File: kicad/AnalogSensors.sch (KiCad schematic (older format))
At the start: 8 parts, among them P201 Positive, P202 Negative

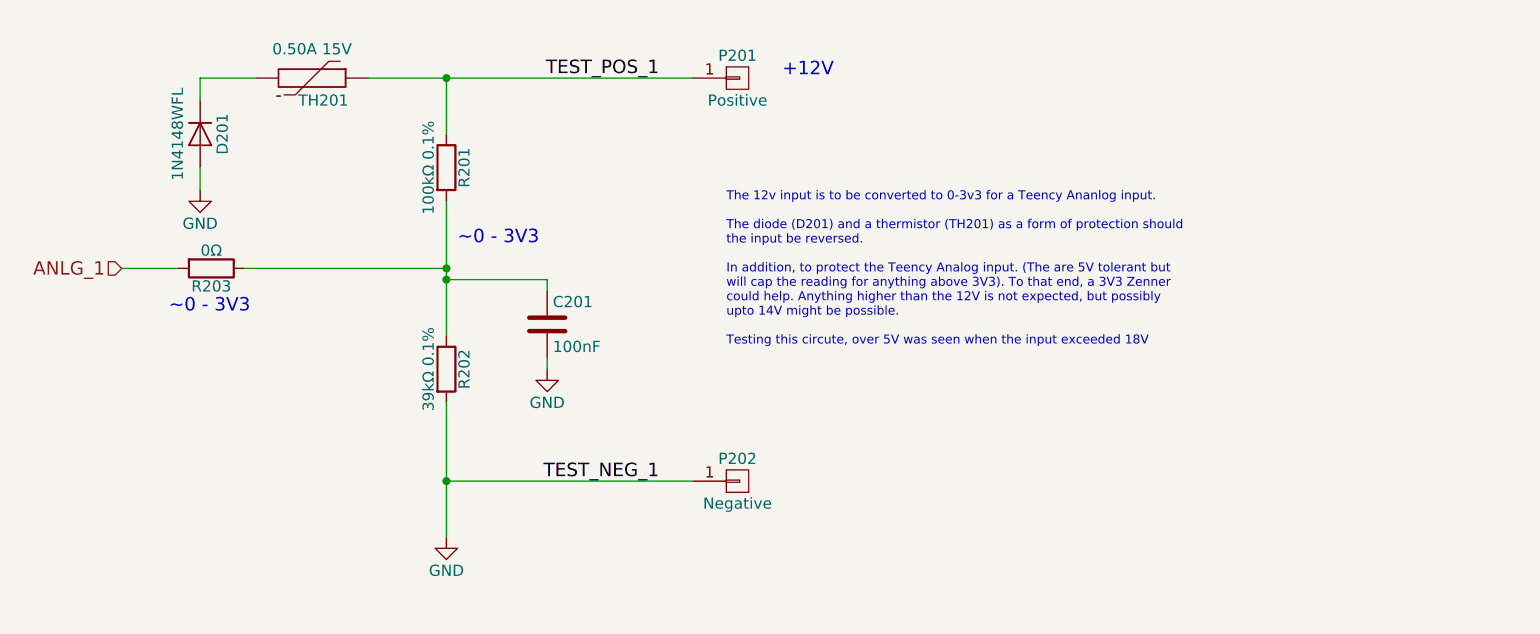
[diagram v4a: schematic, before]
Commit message: Small formatting changes on schematic for Forum questions
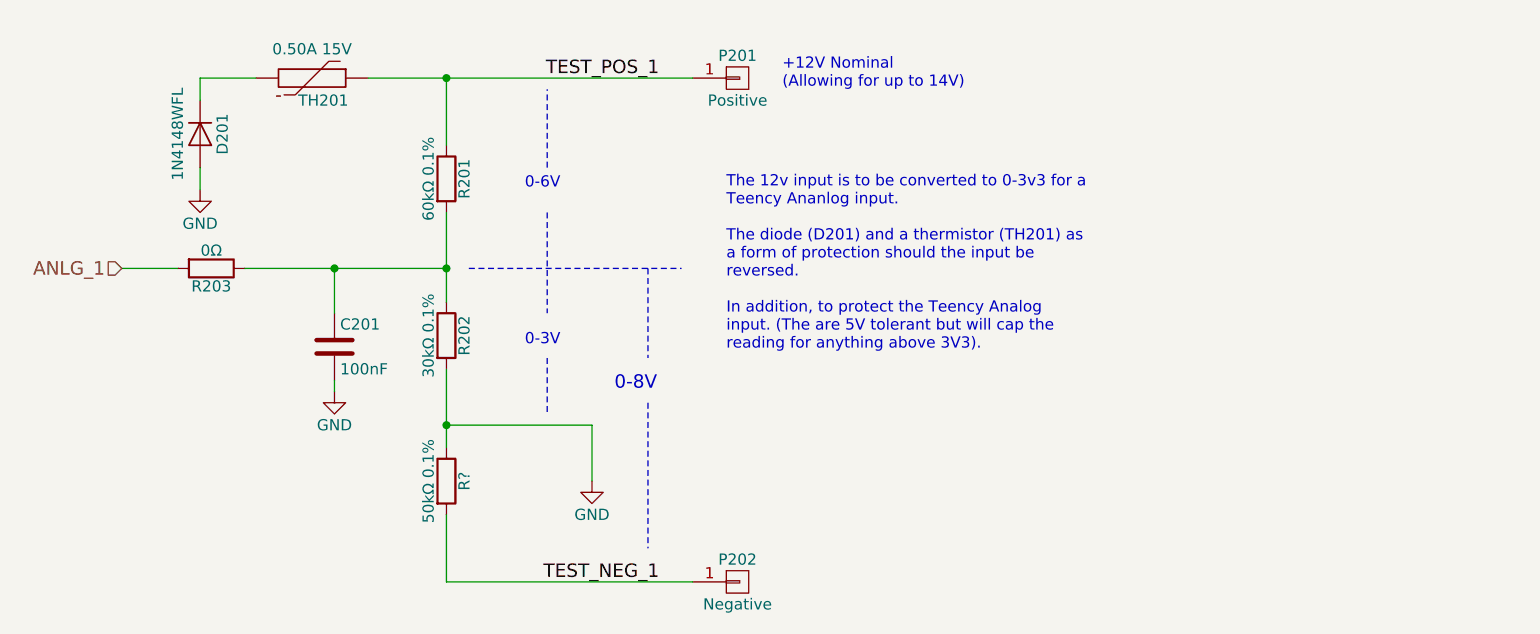
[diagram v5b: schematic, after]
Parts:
- added R?: 50kΩ 0.1%, Resistors_SMD:R_1206, symbol R
- R201: value 100kΩ 0.1% -> 60kΩ 0.1%
- R202: value 39kΩ 0.1% -> 30kΩ 0.1%
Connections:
- net GND: now also R?.1; no longer P202.1 (P1)
- new net TEST_NEG_1: P202.1 (P1), R?.2
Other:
- note added: "+12V Nominal\n(Allowing for up to 14V)"
- note added: "0-3V"
- note added: "0-6V"
- note added: "0-8V"
- note added: "\nThe 12v input is to be converted to 0-3v3 for a \nTeency Ananlog input.\n\nThe diode (D201) and a thermistor (TH201) as \na form of protection should the input be \nreversed.\n\nIn addition, to protect the Teency Analog \ninput. (The are 5V tolerant but will cap the \nreading for anything above 3V3).\n\n"
- note removed: "+12V"
- note removed: "\nThe 12v input is to be converted to 0-3v3 for a Teency Ananlog input.\n\nThe diode (D201) and a thermistor (TH201) as a form of protection should \nthe input be reversed.\n\nIn addition, to protect the Teency Analog input. (The are 5V tolerant but \nwill cap the reading for anything above 3V3). To that end, a 3V3 Zenner \ncould help. Anything higher than the 12V is not expected, but possibly \n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"
- note removed: "~~0 - 3V3"
- moved on the sheet: C201, P202, R201, R202
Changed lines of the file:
@@
 L R R201
 U 1 1 593EDD83
-P 3500 1800
-F 0 "R201" V 3580 1800 50  0000 C CNN
-F 1 "100kΩ 0.1%" V 3420 1800 50  0000 C CNN
-F 2 "Resistors_SMD:R_1206" V 3430 1800 50  0001 C CNN
-F 3 "" H 3500 1800 50  0000 C CNN
-F 4 "SPR-1206 100K" H 3500 1800 60  0001 C CNN "MPN"
-F 5 "Value" H 3500 1800 60  0001 C CNN "Link"
-	1    3500 1800
+P 3500 1850
+F 0 "R201" V 3580 1850 50  0000 C CNN
+F 1 "60kΩ 0.1%" V 3420 1850 50  0000 C CNN
+F 2 "Resistors_SMD:R_1206" V 3430 1850 50  0001 C CNN
+F 3 "" H 3500 1850 50  0000 C CNN
+F 4 "SPR-1206 100K" H 3500 1850 60  0001 C CNN "MPN"
+F 5 "Value" H 3500 1850 60  0001 C CNN "Link"
+	1    3500 1850
 	1    0    0    -1
 $EndComp
@@
 L R R202
 U 1 1 593EDD8A
-P 3500 2700
-F 0 "R202" V 3580 2700 50  0000 C CNN
-F 1 "39kΩ 0.1%" V 3420 2700 50  0000 C CNN
-F 2 "Resistors_SMD:R_1206" V 3430 2700 50  0001 C CNN
-F 3 "" H 3500 2700 50  0000 C CNN
-F 4 "SPR-1206 39,0K" H 3500 2700 60  0001 C CNN "MPN"
-F 5 "Value" H 3500 2700 60  0001 C CNN "Link"
-	1    3500 2700
+P 3500 2550
+F 0 "R202" V 3580 2550 50  0000 C CNN
+F 1 "30kΩ 0.1%" V 3420 2550 50  0000 C CNN
+F 2 "Resistors_SMD:R_1206" V 3430 2550 50  0001 C CNN
+F 3 "" H 3500 2550 50  0000 C CNN
+F 4 "SPR-1206 39,0K" H 3500 2550 60  0001 C CNN "MPN"
+F 5 "Value" H 3500 2550 60  0001 C CNN "Link"
+	1    3500 2550
 	1    0    0    -1
 $EndComp
@@
 L GND #PWR07
 U 1 1 593EDD91
-P 3500 3450
-F 0 "#PWR07" H 3500 3200 50  0001 C CNN
-F 1 "GND" H 3500 3300 50  0000 C CNN
-F 2 "" H 3500 3450 50  0000 C CNN
-F 3 "" H 3500 3450 50  0000 C CNN
-	1    3500 3450
-	1    0    0    -1
-$EndComp
-Text Label 4450 3200 2    60   ~ 0
+P 4150 3200
+F 0 "#PWR07" H 4150 2950 50  0001 C CNN
+F 1 "GND" H 4150 3050 50  0000 C CNN
+F 2 "" H 4150 3200 50  0000 C CNN
+F 3 "" H 4150 3200 50  0000 C CNN
+	1    4150 3200
+	1    0    0    -1
+$EndComp
+Text Label 4450 3650 2    60   ~ 0
 TEST_NEG_1
 Text Label 4450 1400 2    60   ~ 0
@@
 	0    1    1    0
 $EndComp
-Text Notes 5000 1400 0    60   ~ 0
-+12V
-Text Notes 2260 2455 0    60   ~ 0
-~~0 - 3V3
+Text Notes 5000 1450 0    50   ~ 0
++12V Nominal\n(Allowing for up to 14V)
 $Comp
 L C C201
 U 1 1 593EDDC1
-P 3950 2500
-F 0 "C201" H 3975 2600 50  0000 L CNN
-F 1 "100nF" H 3975 2400 50  0000 L CNN
-F 2 "Capacitors_SMD:C_0805" H 3988 2350 30  0001 C CNN
-F 3 "" H 3950 2500 60  0000 C CNN
-	1    3950 2500
+P 3000 2600
+F 0 "C201" H 3025 2700 50  0000 L CNN
+F 1 "100nF" H 3025 2500 50  0000 L CNN
+F 2 "Capacitors_SMD:C_0805" H 3038 2450 30  0001 C CNN
+F 3 "" H 3000 2600 60  0000 C CNN
+	1    3000 2600
 	1    0    0    -1
 $EndComp
@@
 L GND #PWR09
 U 1 1 593EDDCB
-P 3950 2700
-F 0 "#PWR09" H 3950 2450 50  0001 C CNN
-F 1 "GND" H 3950 2550 50  0000 C CNN
-F 2 "" H 3950 2700 50  0000 C CNN
-F 3 "" H 3950 2700 50  0000 C CNN
-	1    3950 2700
+P 3000 2800
+F 0 "#PWR09" H 3000 2550 50  0001 C CNN
+F 1 "GND" H 3000 2650 50  0000 C CNN
+F 2 "" H 3000 2800 50  0000 C CNN
+F 3 "" H 3000 2800 50  0000 C CNN
+	1    3000 2800
 	1    0    0    -1
 $EndComp
@@
 	3150 1400 4600 1400
 Wire Wire Line
-	3500 1400 3500 1650
+	3500 1400 3500 1700
 Connection ~ 3500 1400
 Wire Wire Line
-	3500 1950 3500 2550
-Wire Wire Line
-	3500 2850 3500 3450
-Wire Wire Line
-	3950 2650 3950 2700
-Wire Wire Line
-	3950 2300 3950 2350
-Wire Wire Line
-	3500 3200 4600 3200
-Connection ~ 3500 3200
+	3500 2000 3500 2400
+Wire Wire Line
+	3000 2750 3000 2800
+Wire Wire Line
+	3500 3650 4600 3650
 $Comp
 L CONN_01X01 P201
@@
 L CONN_01X01 P202
 U 1 1 594067C4
-P 4800 3200
-F 0 "P202" H 4800 3300 50  0000 C CNN
-F 1 "Negative" H 4800 3100 50  0000 C CNN
-F 2 "Pin_Headers:Pin_Header_Straight_1x01_Pitch2.54mm" H 4800 3200 60  0001 C CNN
-F 3 "" H 4800 3200 60  0000 C CNN
-	1    4800 3200
+P 4800 3650
+F 0 "P202" H 4800 3750 50  0000 C CNN
+F 1 "Negative" H 4800 3550 50  0000 C CNN
+F 2 "Pin_Headers:Pin_Header_Straight_1x01_Pitch2.54mm" H 4800 3650 60  0001 C CNN
+F 3 "" H 4800 3650 60  0000 C CNN
+	1    4800 3650
 	1    0    0    -1
 $EndComp
@@
 	2600 2250 3500 2250
 Connection ~ 3500 2250
-Wire Wire Line
-	3500 2300 3950 2300
-Connection ~ 3500 2300
-Text Notes 4750 2600 0    40   ~ 0
-\nThe 12v input is to be converted to 0-3v3 for a Teency Ananlog input.\n\nThe diode (D201) and a thermistor (TH201) as a form of protection should \nthe input be reversed.\n\nIn addition, to protect the Teency Analog input. (The are 5V tolerant but \nwill cap the reading for anything above 3V3). To that end, a 3V3 Zenner \ncould help. Anything higher than the 12V is not expected, but possibly \nupto 14V might be possible.\n\nTesting this circute, over 5V was seen when the input exceeded 18V
-Text Notes 3550 2150 0    60   ~ 0
-~~0 - 3V3
+Text Notes 4750 2700 0    50   ~ 0
+\nThe 12v input is to be converted to 0-3v3 for a \nTeency Ananlog input.\n\nThe diode (D201) and a thermistor (TH201) as \na form of protection should the input be \nreversed.\n\nIn addition, to protect the Teency Analog \ninput. (The are 5V tolerant but will cap the \nreading for anything above 3V3).\n\n
+Text Notes 3850 2600 0    50   ~ 0
+0-3V
+$Comp
+L R R?
+U 1 1 599477ED
+P 3500 3200
+F 0 "R?" V 3580 3200 50  0000 C CNN
+F 1 "50kΩ 0.1%" V 3420 3200 50  0000 C CNN
+F 2 "Resistors_SMD:R_1206" V 3430 3200 50  0001 C CNN
+F 3 "" H 3500 3200 50  0000 C CNN
+F 4 "SPR-1206 39,0K" H 3500 3200 60  0001 C CNN "MPN"
+F 5 "Value" H 3500 3200 60  0001 C CNN "Link"
+	1    3500 3200
+	1    0    0    -1
+$EndComp
+Wire Wire Line
+	3500 2700 3500 3050
+Wire Wire Line
+	3500 3350 3500 3650
+Wire Wire Line
+	3500 2950 4150 2950
+Wire Wire Line
+	4150 2950 4150 3200
+Connection ~ 3500 2950
+Wire Wire Line
+	3000 2450 3000 2250
+Connection ~ 3000 2250
+Wire Notes Line
+	4400 2250 4400 2650
+Wire Notes Line
+	4400 2850 4400 3500
+Text Notes 4250 2800 0    60   ~ 0
+0-8V
+Wire Notes Line
+	3600 2250 4550 2250
+Wire Notes Line
+	3950 2000 3950 2450
+Wire Notes Line
+	3950 2650 3950 2900
+Wire Notes Line
+	3950 1800 3950 1450
+Text Notes 3850 1900 0    50   ~ 0
+0-6V
 $EndSCHEMATC

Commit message: Enhanced display port connector and layout - Submit to OSH Park
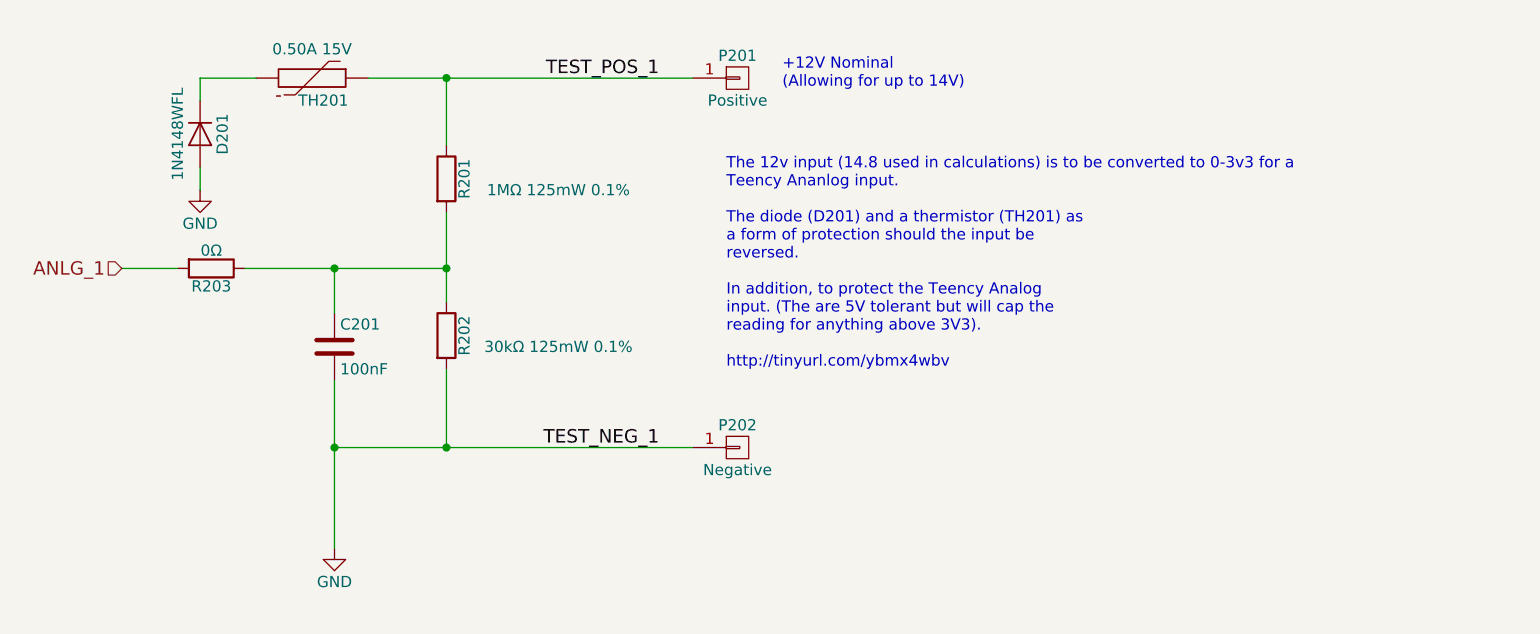
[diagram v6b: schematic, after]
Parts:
- removed R?: 50kΩ 0.1%, Resistors_SMD:R_1206, symbol R
- C201: footprint Capacitors_SMD:C_0805 -> Capacitors_SMD:C_0805_HandSoldering
- R201: value 60kΩ 0.1% -> 1MΩ 125mW 0.1%; footprint Resistors_SMD:R_1206 -> Resistors_SMD:R_1206_HandSoldering
- R202: value 30kΩ 0.1% -> 30kΩ 125mW 0.1%; footprint Resistors_SMD:R_1206 -> Resistors_SMD:R_1206_HandSoldering
- R203: footprint Resistors_SMD:R_0805 -> Resistors_SMD:R_0805_HandSoldering
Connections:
- net TEST_NEG_1 is gone; now on net GND: P202.1 (P1)
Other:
- note added: "\nThe 12v input (14.8 used in calculations) is to be converted to 0-3v3 for a \nTeency Ananlog input.\n\nThe diode (D201) and a thermistor (TH201) as \na form of protection should the input be \nreversed.\n\nIn addition, to protect the Teency Analog \ninput. (The are 5V tolerant but will cap the \nreading for anything above 3V3).\n\nhttp://tinyurl.com/ybmx4wbv"
- note removed: "0-3V"
- note removed: "0-6V"
- note removed: "0-8V"
- note removed: "\nThe 12v input is to be converted to 0-3v3 for a \nTeency Ananlog input.\n\nThe diode (D201) and a thermistor (TH201) as \na form of protection should the input be \nreversed.\n\nIn addition, to protect the Teency Analog \ninput. (The are 5V tolerant but will cap the \nreading for anything above 3V3).\n\n"
- moved on the sheet: P202
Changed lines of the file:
@@
 P 3500 1850
 F 0 "R201" V 3580 1850 50  0000 C CNN
-F 1 "60kΩ 0.1%" V 3420 1850 50  0000 C CNN
-F 2 "Resistors_SMD:R_1206" V 3430 1850 50  0001 C CNN
+F 1 "1MΩ 125mW  0.1%" H 4000 1800 50  0000 C CNN
+F 2 "Resistors_SMD:R_1206_HandSoldering" V 3430 1850 50  0001 C CNN
 F 3 "" H 3500 1850 50  0000 C CNN
 F 4 "SPR-1206 100K" H 3500 1850 60  0001 C CNN "MPN"
@@
 P 3500 2550
 F 0 "R202" V 3580 2550 50  0000 C CNN
-F 1 "30kΩ 0.1%" V 3420 2550 50  0000 C CNN
-F 2 "Resistors_SMD:R_1206" V 3430 2550 50  0001 C CNN
+F 1 "30kΩ 125mW  0.1%" H 4000 2500 50  0000 C CNN
+F 2 "Resistors_SMD:R_1206_HandSoldering" V 3430 2550 50  0001 C CNN
 F 3 "" H 3500 2550 50  0000 C CNN
 F 4 "SPR-1206 39,0K" H 3500 2550 60  0001 C CNN "MPN"
@@
 	1    0    0    -1
 $EndComp
-$Comp
-L GND #PWR07
-U 1 1 593EDD91
-P 4150 3200
-F 0 "#PWR07" H 4150 2950 50  0001 C CNN
-F 1 "GND" H 4150 3050 50  0000 C CNN
-F 2 "" H 4150 3200 50  0000 C CNN
-F 3 "" H 4150 3200 50  0000 C CNN
-	1    4150 3200
-	1    0    0    -1
-$EndComp
-Text Label 4450 3650 2    60   ~ 0
+Text Label 4450 3050 2    60   ~ 0
 TEST_NEG_1
 Text Label 4450 1400 2    60   ~ 0
@@
 F 0 "C201" H 3025 2700 50  0000 L CNN
 F 1 "100nF" H 3025 2500 50  0000 L CNN
-F 2 "Capacitors_SMD:C_0805" H 3038 2450 30  0001 C CNN
+F 2 "Capacitors_SMD:C_0805_HandSoldering" H 3038 2450 30  0001 C CNN
 F 3 "" H 3000 2600 60  0000 C CNN
 	1    3000 2600
@@
 L GND #PWR09
 U 1 1 593EDDCB
-P 3000 2800
-F 0 "#PWR09" H 3000 2550 50  0001 C CNN
-F 1 "GND" H 3000 2650 50  0000 C CNN
-F 2 "" H 3000 2800 50  0000 C CNN
-F 3 "" H 3000 2800 50  0000 C CNN
-	1    3000 2800
+P 3000 3500
+F 0 "#PWR09" H 3000 3250 50  0001 C CNN
+F 1 "GND" H 3000 3350 50  0000 C CNN
+F 2 "" H 3000 3500 50  0000 C CNN
+F 3 "" H 3000 3500 50  0000 C CNN
+	1    3000 3500
 	1    0    0    -1
 $EndComp
@@
 	3500 2000 3500 2400
 Wire Wire Line
-	3000 2750 3000 2800
-Wire Wire Line
-	3500 3650 4600 3650
+	3000 2750 3000 3500
 $Comp
 L CONN_01X01 P201
@@
 L CONN_01X01 P202
 U 1 1 594067C4
-P 4800 3650
-F 0 "P202" H 4800 3750 50  0000 C CNN
-F 1 "Negative" H 4800 3550 50  0000 C CNN
-F 2 "Pin_Headers:Pin_Header_Straight_1x01_Pitch2.54mm" H 4800 3650 60  0001 C CNN
-F 3 "" H 4800 3650 60  0000 C CNN
-	1    4800 3650
+P 4800 3050
+F 0 "P202" H 4800 3150 50  0000 C CNN
+F 1 "Negative" H 4800 2950 50  0000 C CNN
+F 2 "Pin_Headers:Pin_Header_Straight_1x01_Pitch2.54mm" H 4800 3050 60  0001 C CNN
+F 3 "" H 4800 3050 60  0000 C CNN
+	1    4800 3050
 	1    0    0    -1
 $EndComp
@@
 F 0 "R203" V 2530 2250 50  0000 C CNN
 F 1 "0Ω" V 2370 2250 50  0000 C CNN
-F 2 "Resistors_SMD:R_0805" V 2380 2250 50  0001 C CNN
+F 2 "Resistors_SMD:R_0805_HandSoldering" V 2380 2250 50  0001 C CNN
 F 3 "" H 2450 2250 50  0000 C CNN
 F 4 "Value" H 2450 2250 60  0001 C CNN "Link"
@@
 Connection ~ 3500 2250
 Text Notes 4750 2700 0    50   ~ 0
-\nThe 12v input is to be converted to 0-3v3 for a \nTeency Ananlog input.\n\nThe diode (D201) and a thermistor (TH201) as \na form of protection should the input be \nreversed.\n\nIn addition, to protect the Teency Analog \ninput. (The are 5V tolerant but will cap the \nreading for anything above 3V3).\n\n
-Text Notes 3850 2600 0    50   ~ 0
-0-3V
-$Comp
-L R R?
-U 1 1 599477ED
-P 3500 3200
-F 0 "R?" V 3580 3200 50  0000 C CNN
-F 1 "50kΩ 0.1%" V 3420 3200 50  0000 C CNN
-F 2 "Resistors_SMD:R_1206" V 3430 3200 50  0001 C CNN
-F 3 "" H 3500 3200 50  0000 C CNN
-F 4 "SPR-1206 39,0K" H 3500 3200 60  0001 C CNN "MPN"
-F 5 "Value" H 3500 3200 60  0001 C CNN "Link"
-	1    3500 3200
-	1    0    0    -1
-$EndComp
-Wire Wire Line
-	3500 2700 3500 3050
-Wire Wire Line
-	3500 3350 3500 3650
-Wire Wire Line
-	3500 2950 4150 2950
-Wire Wire Line
-	4150 2950 4150 3200
-Connection ~ 3500 2950
+\nThe 12v input (14.8 used in calculations) is to be converted to 0-3v3 for a \nTeency Ananlog input.\n\nThe diode (D201) and a thermistor (TH201) as \na form of protection should the input be \nreversed.\n\nIn addition, to protect the Teency Analog \ninput. (The are 5V tolerant but will cap the \nreading for anything above 3V3).\n\nhttp://tinyurl.com/ybmx4wbv
 Wire Wire Line
 	3000 2450 3000 2250
 Connection ~ 3000 2250
-Wire Notes Line
-	4400 2250 4400 2650
-Wire Notes Line
-	4400 2850 4400 3500
-Text Notes 4250 2800 0    60   ~ 0
-0-8V
-Wire Notes Line
-	3600 2250 4550 2250
-Wire Notes Line
-	3950 2000 3950 2450
-Wire Notes Line
-	3950 2650 3950 2900
-Wire Notes Line
-	3950 1800 3950 1450
-Text Notes 3850 1900 0    50   ~ 0
-0-6V
+Wire Wire Line
+	3500 3050 3500 2700
+Wire Wire Line
+	3000 3050 4600 3050
+Connection ~ 3000 3050
+Connection ~ 3500 3050
 $EndSCHEMATC

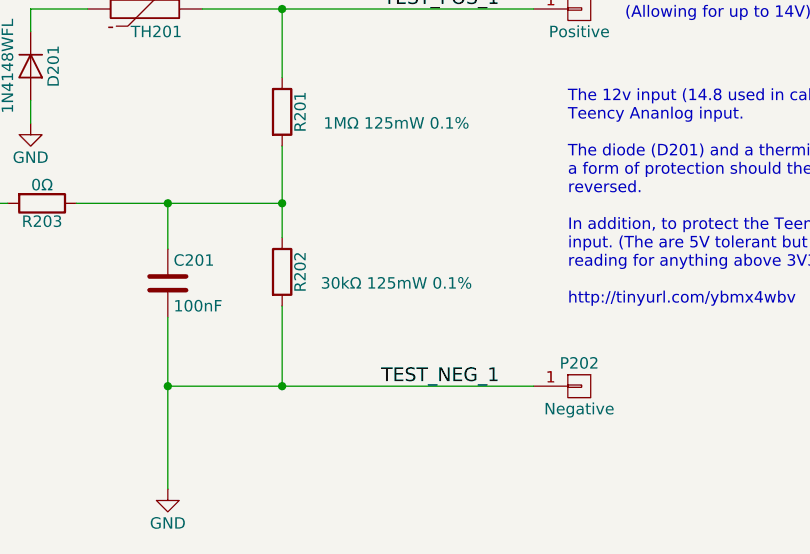
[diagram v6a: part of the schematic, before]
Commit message: Added test code to drive the LCD display
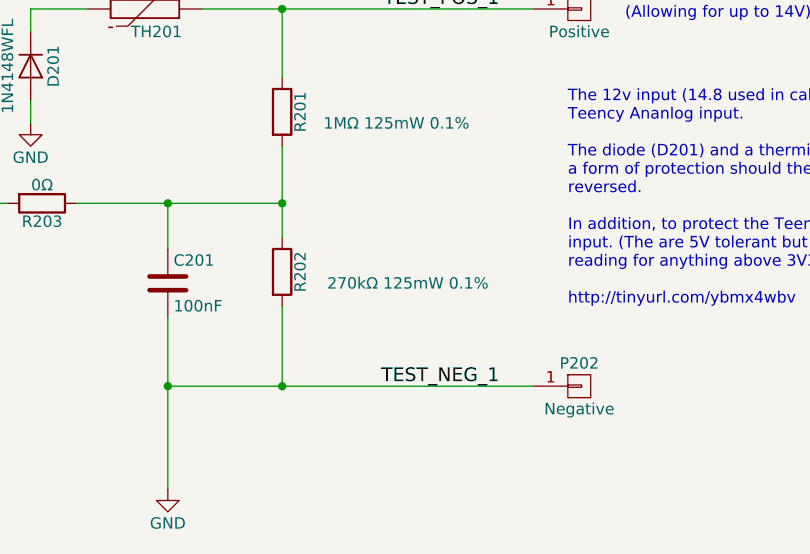
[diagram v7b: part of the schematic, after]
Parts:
- R202: value 30kΩ 125mW 0.1% -> 270kΩ 125mW 0.1%
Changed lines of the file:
@@
 P 3500 2550
 F 0 "R202" V 3580 2550 50  0000 C CNN
-F 1 "30kΩ 125mW  0.1%" H 4000 2500 50  0000 C CNN
+F 1 "270kΩ 125mW  0.1%" H 4050 2500 50  0000 C CNN
 F 2 "Resistors_SMD:R_1206_HandSoldering" V 3430 2550 50  0001 C CNN
 F 3 "" H 3500 2550 50  0000 C CNN
